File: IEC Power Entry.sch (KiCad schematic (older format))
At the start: 9 parts, among them J1 Transformer Primary, P1 MountingHole_Pad, P2 Chassis Ground

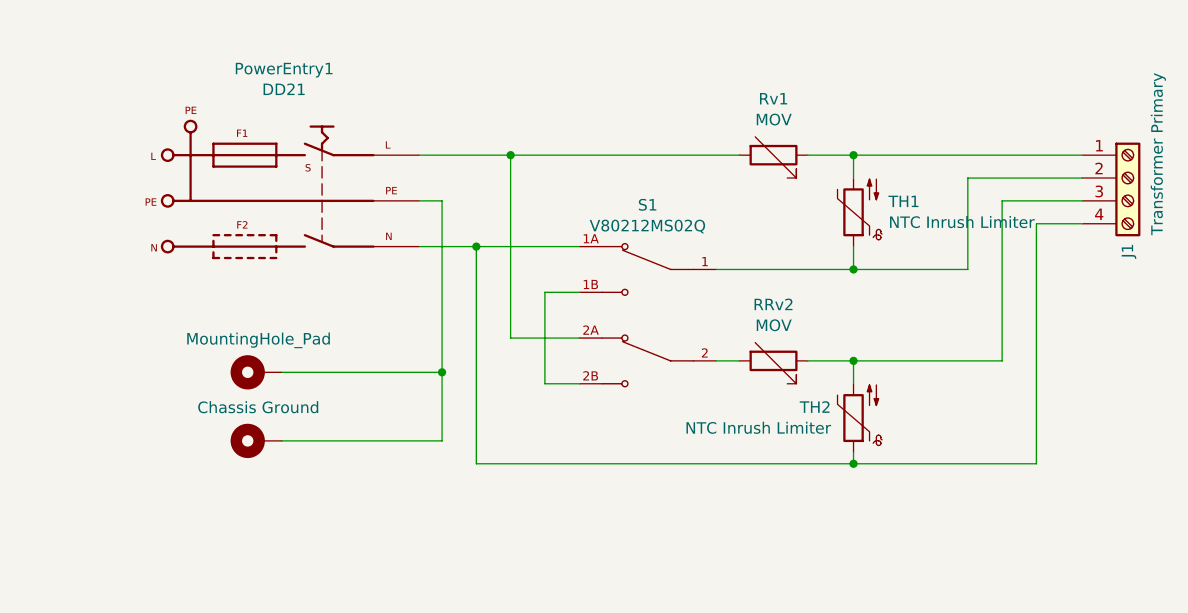
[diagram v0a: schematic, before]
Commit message: fix: correct mov and inrush placement
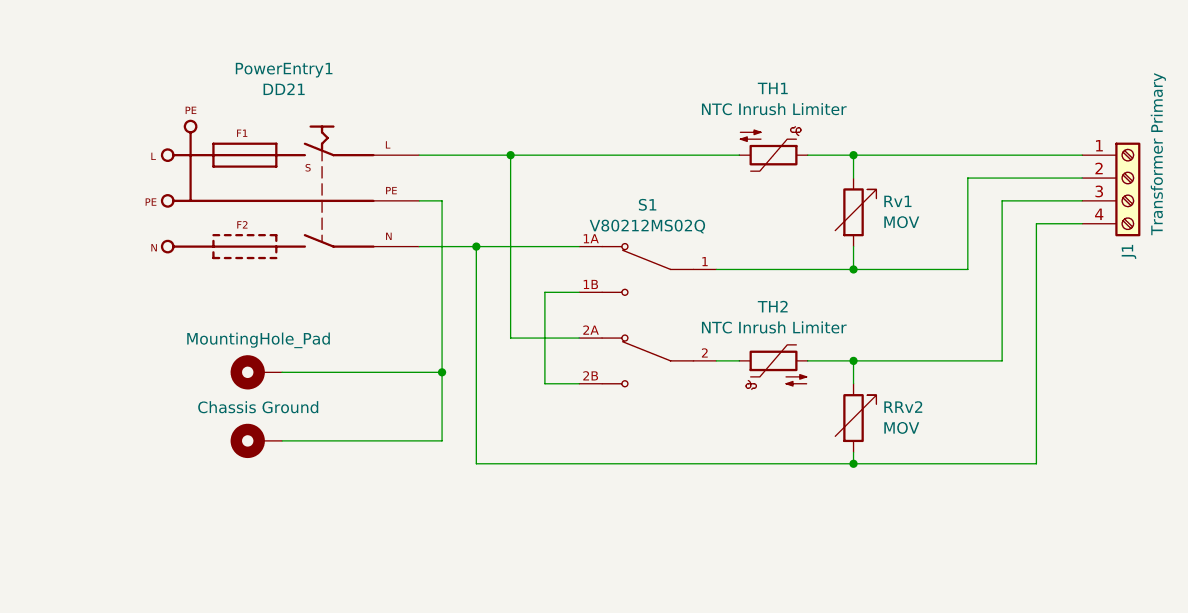
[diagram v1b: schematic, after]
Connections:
- net at PowerEntry1.L, S1.2A: now also TH1.2; no longer Rv1.2
- net at J1.4 (Pin_4), PowerEntry1.N, S1.1A: now also RRv2.2; no longer TH2.1
- net at J1.2 (Pin_2), S1.1: now also Rv1.2; no longer TH1.1
- net at S1.2: now also TH2.1; no longer RRv2.2
- net at J1.1 (Pin_1), Rv1.1: now also TH1.1; no longer TH1.2
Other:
- moved on the sheet: RRv2, Rv1, TH1, TH2
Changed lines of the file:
@@
 L Device:Thermistor_NTC TH1
 U 1 1 5F3C2FF6
-P 6600 3500
-F 0 "TH1" H 6447 3454 50  0000 R CNN
-F 1 "NTC Inrush Limiter" H 6447 3545 50  0000 R CNN
-F 2 "Varistor:RV_Disc_D9mm_W6.1mm_P5mm" H 6600 3550 50  0001 C CNN
-F 3 "~" H 6600 3550 50  0001 C CNN
-	1    6600 3500
-	-1   0    0    1
+P 6250 3250
+F 0 "TH1" V 5960 3250 50  0000 C CNN
+F 1 "NTC Inrush Limiter" V 6051 3250 50  0000 C CNN
+F 2 "Varistor:RV_Disc_D9mm_W6.1mm_P5mm" H 6250 3300 50  0001 C CNN
+F 3 "~" H 6250 3300 50  0001 C CNN
+	1    6250 3250
+	0    1    1    0
 $EndComp
 $Comp
 L Device:R_Variable Rv1
 U 1 1 5F3CD17B
-P 6250 3250
-F 0 "Rv1" V 6005 3250 50  0000 C CNN
-F 1 "MOV" V 6096 3250 50  0000 C CNN
-F 2 "Varistor:RV_Disc_D9mm_W6.1mm_P5mm" V 6180 3250 50  0001 C CNN
-F 3 "~" H 6250 3250 50  0001 C CNN
-	1    6250 3250
-	0    1    1    0
+P 6600 3500
+F 0 "Rv1" H 6728 3546 50  0000 L CNN
+F 1 "MOV" H 6728 3455 50  0000 L CNN
+F 2 "Varistor:RV_Disc_D9mm_W6.1mm_P5mm" V 6530 3500 50  0001 C CNN
+F 3 "~" H 6600 3500 50  0001 C CNN
+	1    6600 3500
+	1    0    0    -1
 $EndComp
 $Comp
@@
 L Device:Thermistor_NTC TH2
 U 1 1 5F3D568E
-P 6600 4400
-F 0 "TH2" H 6698 4354 50  0000 L CNN
-F 1 "NTC Inrush Limiter" H 6698 4445 50  0000 L CNN
-F 2 "Varistor:RV_Disc_D9mm_W6.1mm_P5mm" H 6600 4450 50  0001 C CNN
-F 3 "~" H 6600 4450 50  0001 C CNN
-	1    6600 4400
-	-1   0    0    1
+P 6250 4150
+F 0 "TH2" V 6485 4150 50  0000 C CNN
+F 1 "NTC Inrush Limiter" V 6394 4150 50  0000 C CNN
+F 2 "Varistor:RV_Disc_D9mm_W6.1mm_P5mm" H 6250 4200 50  0001 C CNN
+F 3 "~" H 6250 4200 50  0001 C CNN
+	1    6250 4150
+	0    -1   -1   0
 $EndComp
 $Comp
 L Device:R_Variable RRv2
 U 1 1 5F3D7E0C
-P 6250 4150
-F 0 "RRv2" V 6005 4150 50  0000 C CNN
-F 1 "MOV" V 6096 4150 50  0000 C CNN
-F 2 "Varistor:RV_Disc_D9mm_W6.1mm_P5mm" V 6180 4150 50  0001 C CNN
-F 3 "~" H 6250 4150 50  0001 C CNN
-	1    6250 4150
-	0    1    1    0
+P 6600 4400
+F 0 "RRv2" H 6728 4446 50  0000 L CNN
+F 1 "MOV" H 6728 4355 50  0000 L CNN
+F 2 "Varistor:RV_Disc_D9mm_W6.1mm_P5mm" V 6530 4400 50  0001 C CNN
+F 3 "~" H 6600 4400 50  0001 C CNN
+	1    6600 4400
+	1    0    0    -1
 $EndComp
 Wire Wire Line

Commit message: various updates to track widths and footprints
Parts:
- removed PowerEntry1: DD21, DD21.0121:SCHURTER_DD21.0121.1111, symbol DD21.0121.1111:DD21.0121.1111
- added P3: DD21.0121.1111, Base on Mars Additions:SCHURTER-DD21.0121.1111, symbol DD21.0121.1111:DD21.0121.1111
- J1: footprint TerminalBlock_RND:TerminalBlock_RND_205-00289_1x04_P5.08mm_Horizontal -> TerminalBlock_TE-Connectivity:TerminalBlock_TE_1776266-4_1x4_P5mm_Horizonatal
- MOV1: renamed from Rv1; footprint Varistor:RV_Disc_D9mm_W6.1mm_P5mm -> Base on Mars Additions:V150LA2PX2855
- MOV2: renamed from RRv2; footprint Varistor:RV_Disc_D9mm_W6.1mm_P5mm -> Base on Mars Additions:V150LA2PX2855
- S1: footprint V80212MS02Q:SW_V80212MS02Q -> Base on Mars Additions:SW_V80212MS02Q
- TH1, TH2: footprint Varistor:RV_Disc_D9mm_W6.1mm_P5mm -> Base on Mars Additions:Thermistor_D8.5mm_W6mm_P5MM
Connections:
- net labels added: AC, Earth, Earth_Protective
- wire segments 34 -> 41
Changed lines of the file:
@@
 P 5700 3950
 F 0 "S1" H 5700 4431 50  0000 C CNN
-F 1 "V80212MS02Q" H 5700 4340 50  0000 C CNN
-F 2 "V80212MS02Q:SW_V80212MS02Q" H 5700 3950 50  0001 L BNN
+F 1 "V80212MS02Q" H 5700 4340 50  0001 C CNN
+F 2 "Base on Mars Additions:SW_V80212MS02Q" H 5700 3950 50  0001 L BNN
 F 3 "C&K" H 5700 3950 50  0001 L BNN
 F 4 "N/A" H 5700 3950 50  0001 L BNN "Field4"
@@
 F 0 "TH1" V 5960 3250 50  0000 C CNN
 F 1 "NTC Inrush Limiter" V 6051 3250 50  0000 C CNN
-F 2 "Varistor:RV_Disc_D9mm_W6.1mm_P5mm" H 6250 3300 50  0001 C CNN
+F 2 "Base on Mars Additions:Thermistor_D8.5mm_W6mm_P5MM" H 6250 3300 50  0001 C CNN
 F 3 "~" H 6250 3300 50  0001 C CNN
 	1    6250 3250
@@
 $EndComp
 $Comp
-L Device:R_Variable Rv1
+L Device:R_Variable MOV1
 U 1 1 5F3CD17B
 P 6600 3500
-F 0 "Rv1" H 6728 3546 50  0000 L CNN
-F 1 "MOV" H 6728 3455 50  0000 L CNN
-F 2 "Varistor:RV_Disc_D9mm_W6.1mm_P5mm" V 6530 3500 50  0001 C CNN
+F 0 "MOV1" H 6728 3546 50  0000 L CNN
+F 1 "MOV" H 6728 3455 50  0001 L CNN
+F 2 "Base on Mars Additions:V150LA2PX2855" V 6530 3500 50  0001 C CNN
 F 3 "~" H 6600 3500 50  0001 C CNN
 	1    6600 3500
@@
 L Connector:Screw_Terminal_01x04 J1
 U 1 1 5F3D1820
-P 7800 3350
-F 0 "J1" V 7800 3000 50  0000 L CNN
-F 1 "Transformer Primary" V 7900 3100 50  0000 L TNN
-F 2 "TerminalBlock_RND:TerminalBlock_RND_205-00289_1x04_P5.08mm_Horizontal" H 7800 3350 50  0001 C CNN
-F 3 "~" H 7800 3350 50  0001 C CNN
-	1    7800 3350
-	1    0    0    -1
-$EndComp
-$Comp
-L DD21.0121.1111:DD21.0121.1111 PowerEntry1
-U 1 1 5F3BAA35
-P 4100 3450
-F 0 "PowerEntry1" H 4109 4027 50  0000 C CNN
-F 1 "DD21" H 4109 3936 50  0000 C CNN
-F 2 "DD21.0121:SCHURTER_DD21.0121.1111" H 4100 3450 50  0001 L BNN
-F 3 "Schurter" H 4100 3450 50  0001 L BNN
-	1    4100 3450
-	1    0    0    -1
+P 7800 3450
+F 0 "J1" V 7800 3100 50  0000 L CNN
+F 1 "Transformer Primary" V 7900 3200 50  0000 L TNN
+F 2 "TerminalBlock_TE-Connectivity:TerminalBlock_TE_1776266-4_1x4_P5mm_Horizonatal" H 7800 3450 50  0001 C CNN
+F 3 "~" H 7800 3450 50  0001 C CNN
+	1    7800 3450
+	1    0    0    1
 $EndComp
 $Comp
@@
 F 0 "TH2" V 6485 4150 50  0000 C CNN
 F 1 "NTC Inrush Limiter" V 6394 4150 50  0000 C CNN
-F 2 "Varistor:RV_Disc_D9mm_W6.1mm_P5mm" H 6250 4200 50  0001 C CNN
+F 2 "Base on Mars Additions:Thermistor_D8.5mm_W6mm_P5MM" H 6250 4200 50  0001 C CNN
 F 3 "~" H 6250 4200 50  0001 C CNN
 	1    6250 4150
@@
 $EndComp
 $Comp
-L Device:R_Variable RRv2
+L Device:R_Variable MOV2
 U 1 1 5F3D7E0C
 P 6600 4400
-F 0 "RRv2" H 6728 4446 50  0000 L CNN
-F 1 "MOV" H 6728 4355 50  0000 L CNN
-F 2 "Varistor:RV_Disc_D9mm_W6.1mm_P5mm" V 6530 4400 50  0001 C CNN
+F 0 "MOV2" H 6728 4446 50  0000 L CNN
+F 1 "MOV" H 6728 4355 50  0001 L CNN
+F 2 "Base on Mars Additions:V150LA2PX2855" V 6530 4400 50  0001 C CNN
 F 3 "~" H 6600 4400 50  0001 C CNN
 	1    6600 4400
@@
 	4800 4500 4800 4200
 Connection ~ 4800 4200
+$Comp
+L power:Earth_Protective #PWR02
+U 1 1 5F407098
+P 3325 3750
+F 0 "#PWR02" H 3325 3500 50  0001 C CNN
+F 1 "Earth_Protective" H 3325 3600 50  0001 C CNN
+F 2 "" H 3325 3750 50  0001 C CNN
+F 3 "~" H 3325 3750 50  0001 C CNN
+	1    3325 3750
+	1    0    0    -1
+$EndComp
+Wire Wire Line
+	3325 3450 3600 3450
+$Comp
+L power:Earth #PWR03
+U 1 1 5F40A4DC
+P 3600 3850
+F 0 "#PWR03" H 3600 3600 50  0001 C CNN
+F 1 "Earth" H 3600 3700 50  0001 C CNN
+F 2 "" H 3600 3850 50  0001 C CNN
+F 3 "~" H 3600 3850 50  0001 C CNN
+	1    3600 3850
+	1    0    0    -1
+$EndComp
+Wire Wire Line
+	3600 3650 3600 3850
+Wire Wire Line
+	3700 3125 3325 3125
+Wire Wire Line
+	3325 3125 3325 3450
+Connection ~ 3325 3450
+Wire Wire Line
+	3325 3450 3325 3750
+$Comp
+L power:AC #PWR01
+U 1 1 5F40D02A
+P 3025 3775
+F 0 "#PWR01" H 3025 3675 50  0001 C CNN
+F 1 "AC" H 3025 4050 50  0000 C CNN
+F 2 "" H 3025 3775 50  0001 C CNN
+F 3 "" H 3025 3775 50  0001 C CNN
+	1    3025 3775
+	-1   0    0    1
+$EndComp
+Wire Wire Line
+	3025 3250 3600 3250
+Wire Wire Line
+	3025 3250 3025 3750
+$Comp
+L DD21.0121.1111:DD21.0121.1111 P3
+U 1 1 5F4000A5
+P 4100 3450
+F 0 "P3" H 4109 3935 50  0000 C CNN
+F 1 "DD21.0121.1111" H 4109 4026 50  0001 C CNN
+F 2 "Base on Mars Additions:SCHURTER-DD21.0121.1111" H 4109 3935 50  0001 C CNN
+F 3 "Schurter" H 4100 3450 50  0001 L BNN
+	1    4100 3450
+	1    0    0    -1
+$EndComp
 $EndSCHEMATC

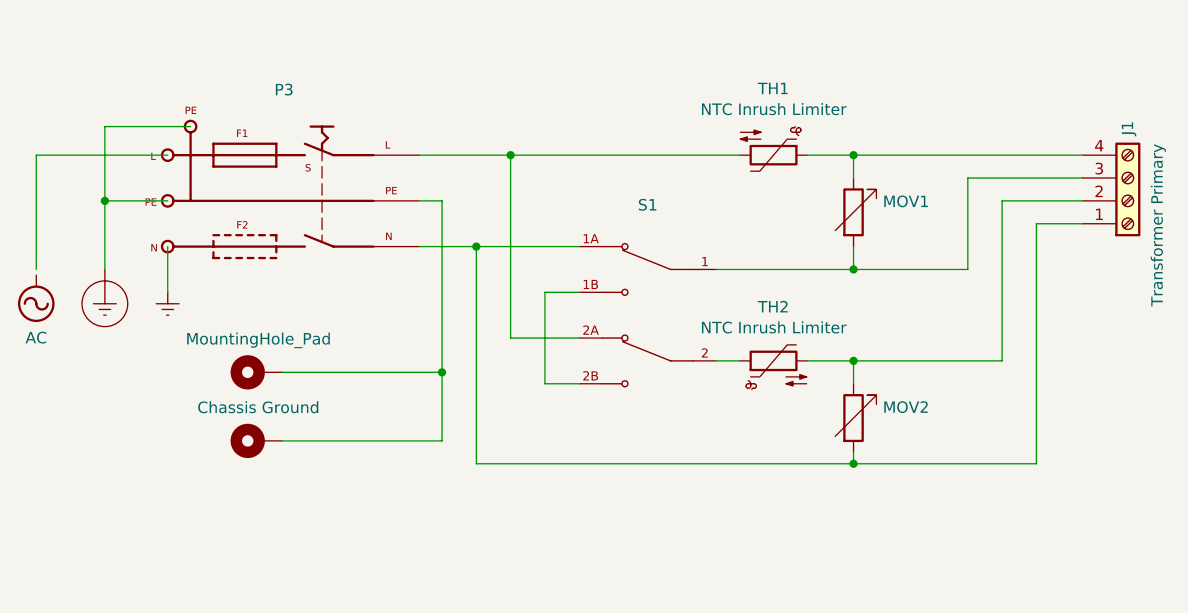
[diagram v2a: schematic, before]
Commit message: feat: more track layout tweaking
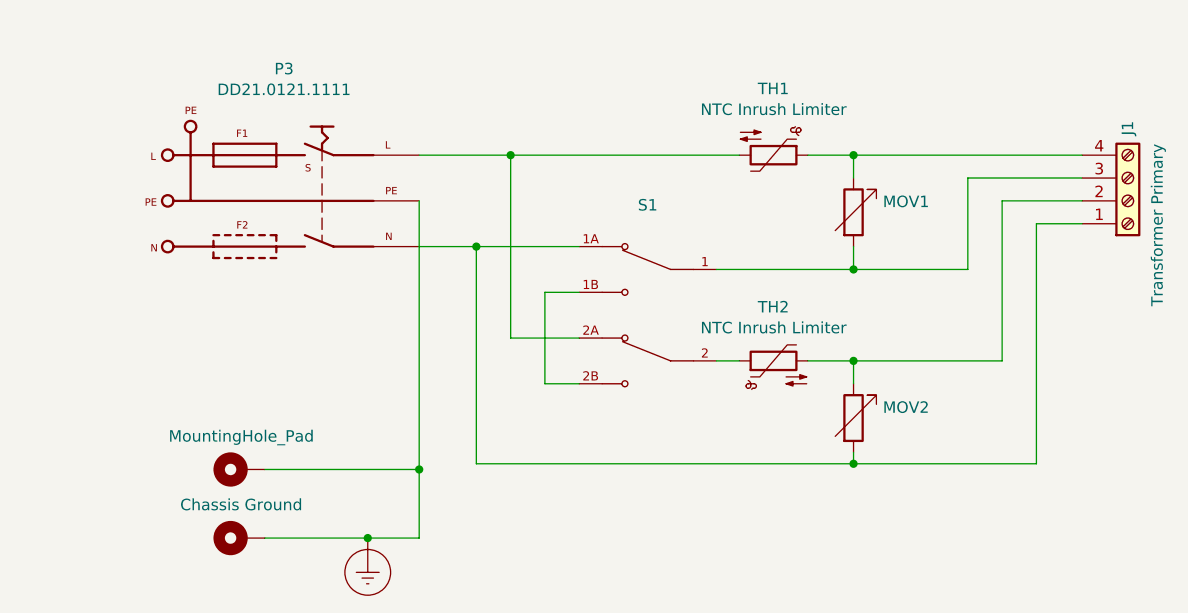
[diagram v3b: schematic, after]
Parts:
- J1: footprint TerminalBlock_TE-Connectivity:TerminalBlock_TE_1776266-4_1x4_P5mm_Horizonatal -> TerminalBlock_TE-Connectivity:TerminalBlock_TE-1546062-4_1x04_P7.50mm_Horizontal
- MOV1, MOV2: footprint Base on Mars Additions:V150LA2PX2855 -> Varistor:RV_Disc_D12mm_W5mm_P7.5mm
- P1: footprint MountingHole:MountingHole_4.3mm_M4_Pad -> MountingHole:MountingHole_3.5mm_Pad
- P2: footprint MountingHole:MountingHole_3.2mm_M3_Pad -> MountingHole:MountingHole_3.5mm_Pad
- TH1, TH2: footprint Base on Mars Additions:Thermistor_D8.5mm_W6mm_P5MM -> Varistor:RV_Disc_D12mm_W7.1mm_P7.5mm
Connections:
- net labels removed: AC, Earth
- wire segments 41 -> 34
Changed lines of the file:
@@
 F 0 "TH1" V 5960 3250 50  0000 C CNN
 F 1 "NTC Inrush Limiter" V 6051 3250 50  0000 C CNN
-F 2 "Base on Mars Additions:Thermistor_D8.5mm_W6mm_P5MM" H 6250 3300 50  0001 C CNN
+F 2 "Varistor:RV_Disc_D12mm_W7.1mm_P7.5mm" H 6250 3300 50  0001 C CNN
 F 3 "~" H 6250 3300 50  0001 C CNN
 	1    6250 3250
@@
 F 0 "MOV1" H 6728 3546 50  0000 L CNN
 F 1 "MOV" H 6728 3455 50  0001 L CNN
-F 2 "Base on Mars Additions:V150LA2PX2855" V 6530 3500 50  0001 C CNN
+F 2 "Varistor:RV_Disc_D12mm_W5mm_P7.5mm" V 6530 3500 50  0001 C CNN
 F 3 "~" H 6600 3500 50  0001 C CNN
 	1    6600 3500
 	1    0    0    -1
-$EndComp
-$Comp
-L Connector:Screw_Terminal_01x04 J1
-U 1 1 5F3D1820
-P 7800 3450
-F 0 "J1" V 7800 3100 50  0000 L CNN
-F 1 "Transformer Primary" V 7900 3200 50  0000 L TNN
-F 2 "TerminalBlock_TE-Connectivity:TerminalBlock_TE_1776266-4_1x4_P5mm_Horizonatal" H 7800 3450 50  0001 C CNN
-F 3 "~" H 7800 3450 50  0001 C CNN
-	1    7800 3450
-	1    0    0    1
 $EndComp
 $Comp
@@
 F 0 "TH2" V 6485 4150 50  0000 C CNN
 F 1 "NTC Inrush Limiter" V 6394 4150 50  0000 C CNN
-F 2 "Base on Mars Additions:Thermistor_D8.5mm_W6mm_P5MM" H 6250 4200 50  0001 C CNN
+F 2 "Varistor:RV_Disc_D12mm_W7.1mm_P7.5mm" H 6250 4200 50  0001 C CNN
 F 3 "~" H 6250 4200 50  0001 C CNN
 	1    6250 4150
@@
 F 0 "MOV2" H 6728 4446 50  0000 L CNN
 F 1 "MOV" H 6728 4355 50  0001 L CNN
-F 2 "Base on Mars Additions:V150LA2PX2855" V 6530 4400 50  0001 C CNN
+F 2 "Varistor:RV_Disc_D12mm_W5mm_P7.5mm" V 6530 4400 50  0001 C CNN
 F 3 "~" H 6600 4400 50  0001 C CNN
 	1    6600 4400
@@
 	6600 4600 7400 4600
 Wire Wire Line
-	4700 3450 4800 3450
-Wire Wire Line
 	4700 3250 5100 3250
 Wire Wire Line
-	4700 3650 4950 3650
-Wire Wire Line
-	4950 3650 4950 4600
-Wire Wire Line
 	4950 4600 6600 4600
-Connection ~ 4950 3650
-Wire Wire Line
-	4950 3650 5400 3650
 Connection ~ 6600 4600
 $Comp
 L Mechanical:MountingHole_Pad P2
 U 1 1 5F3FB5FA
-P 4000 4500
-F 0 "P2" V 4046 4650 50  0001 L CNN
-F 1 "Chassis Ground" V 4145 4503 50  0000 C CNN
-F 2 "MountingHole:MountingHole_3.2mm_M3_Pad" H 4000 4500 50  0001 C CNN
-F 3 "~" H 4000 4500 50  0001 C CNN
-	1    4000 4500
+P 3925 4925
+F 0 "P2" V 3971 5075 50  0001 L CNN
+F 1 "Chassis Ground" V 4070 4928 50  0000 C CNN
+F 2 "MountingHole:MountingHole_3.5mm_Pad" H 3925 4925 50  0001 C CNN
+F 3 "~" H 3925 4925 50  0001 C CNN
+	1    3925 4925
 	0    -1   -1   0
 $EndComp
@@
 L Mechanical:MountingHole_Pad P1
 U 1 1 5F3FBEF4
-P 4000 4200
-F 0 "P1" V 4237 4203 50  0001 C CNN
-F 1 "MountingHole_Pad" V 4145 4203 50  0000 C CNN
-F 2 "MountingHole:MountingHole_4.3mm_M4_Pad" H 4000 4200 50  0001 C CNN
-F 3 "~" H 4000 4200 50  0001 C CNN
-	1    4000 4200
+P 3925 4625
+F 0 "P1" V 4162 4628 50  0001 C CNN
+F 1 "MountingHole_Pad" V 4070 4628 50  0000 C CNN
+F 2 "MountingHole:MountingHole_3.5mm_Pad" H 3925 4625 50  0001 C CNN
+F 3 "~" H 3925 4625 50  0001 C CNN
+	1    3925 4625
 	0    -1   -1   0
 $EndComp
 Wire Wire Line
-	4100 4200 4800 4200
+	4025 4625 4700 4625
 Wire Wire Line
-	4800 3450 4800 4200
+	4025 4925 4475 4925
 Wire Wire Line
-	4100 4500 4800 4500
-Wire Wire Line
-	4800 4500 4800 4200
-Connection ~ 4800 4200
+	4700 4925 4700 4625
 $Comp
 L power:Earth_Protective #PWR02
 U 1 1 5F407098
-P 3325 3750
-F 0 "#PWR02" H 3325 3500 50  0001 C CNN
-F 1 "Earth_Protective" H 3325 3600 50  0001 C CNN
-F 2 "" H 3325 3750 50  0001 C CNN
-F 3 "~" H 3325 3750 50  0001 C CNN
-	1    3325 3750
+P 4475 4925
+F 0 "#PWR02" H 4475 4675 50  0001 C CNN
+F 1 "Earth_Protective" H 4475 4775 50  0001 C CNN
+F 2 "" H 4475 4925 50  0001 C CNN
+F 3 "~" H 4475 4925 50  0001 C CNN
+	1    4475 4925
 	1    0    0    -1
 $EndComp
-Wire Wire Line
-	3325 3450 3600 3450
-$Comp
-L power:Earth #PWR03
-U 1 1 5F40A4DC
-P 3600 3850
-F 0 "#PWR03" H 3600 3600 50  0001 C CNN
-F 1 "Earth" H 3600 3700 50  0001 C CNN
-F 2 "" H 3600 3850 50  0001 C CNN
-F 3 "~" H 3600 3850 50  0001 C CNN
-	1    3600 3850
-	1    0    0    -1
-$EndComp
-Wire Wire Line
-	3600 3650 3600 3850
-Wire Wire Line
-	3700 3125 3325 3125
-Wire Wire Line
-	3325 3125 3325 3450
-Connection ~ 3325 3450
-Wire Wire Line
-	3325 3450 3325 3750
-$Comp
-L power:AC #PWR01
-U 1 1 5F40D02A
-P 3025 3775
-F 0 "#PWR01" H 3025 3675 50  0001 C CNN
-F 1 "AC" H 3025 4050 50  0000 C CNN
-F 2 "" H 3025 3775 50  0001 C CNN
-F 3 "" H 3025 3775 50  0001 C CNN
-	1    3025 3775
-	-1   0    0    1
-$EndComp
-Wire Wire Line
-	3025 3250 3600 3250
-Wire Wire Line
-	3025 3250 3025 3750
 $Comp
 L DD21.0121.1111:DD21.0121.1111 P3
-U 1 1 5F4000A5
+U 1 1 5F496C93
 P 4100 3450
-F 0 "P3" H 4109 3935 50  0000 C CNN
-F 1 "DD21.0121.1111" H 4109 4026 50  0001 C CNN
-F 2 "Base on Mars Additions:SCHURTER-DD21.0121.1111" H 4109 3935 50  0001 C CNN
+F 0 "P3" H 4109 4027 50  0000 C CNN
+F 1 "DD21.0121.1111" H 4109 3936 50  0000 C CNN
+F 2 "Base on Mars Additions:SCHURTER-DD21.0121.1111" H 4100 3450 50  0001 L BNN
 F 3 "Schurter" H 4100 3450 50  0001 L BNN
 	1    4100 3450
 	1    0    0    -1
 $EndComp
+Wire Wire Line
+	4950 3650 4950 4600
+Wire Wire Line
+	4950 3650 5400 3650
+Connection ~ 4475 4925
+Wire Wire Line
+	4475 4925 4700 4925
+Connection ~ 4700 4625
+Connection ~ 4950 3650
+Wire Wire Line
+	4700 3650 4950 3650
+Wire Wire Line
+	4700 3450 4700 4625
+$Comp
+L Connector:Screw_Terminal_01x04 J1
+U 1 1 5F3D1820
+P 7800 3450
+F 0 "J1" V 7800 3100 50  0000 L CNN
+F 1 "Transformer Primary" V 7900 3200 50  0000 L TNN
+F 2 "TerminalBlock_TE-Connectivity:TerminalBlock_TE-1546062-4_1x04_P7.50mm_Horizontal" H 7800 3450 50  0001 C CNN
+F 3 "~" H 7800 3450 50  0001 C CNN
+	1    7800 3450
+	1    0    0    1
+$EndComp
 $EndSCHEMATC
